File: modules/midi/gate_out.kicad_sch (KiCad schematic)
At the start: 5 parts

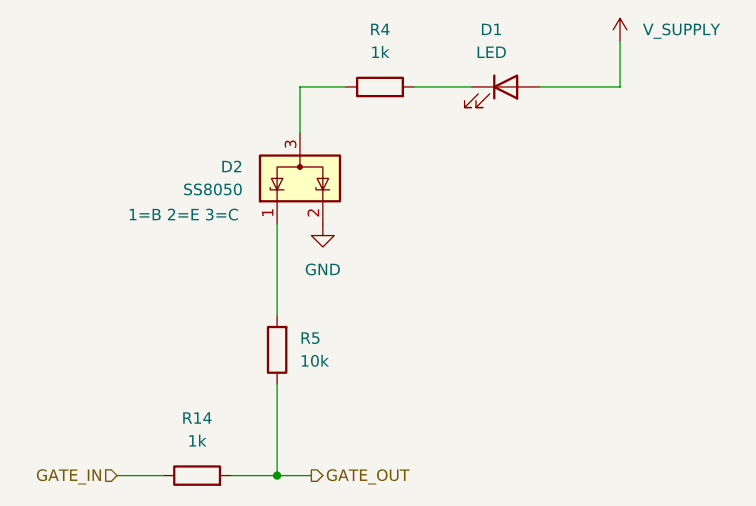
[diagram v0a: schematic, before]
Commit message: midi: Add support to select MIDI A or B
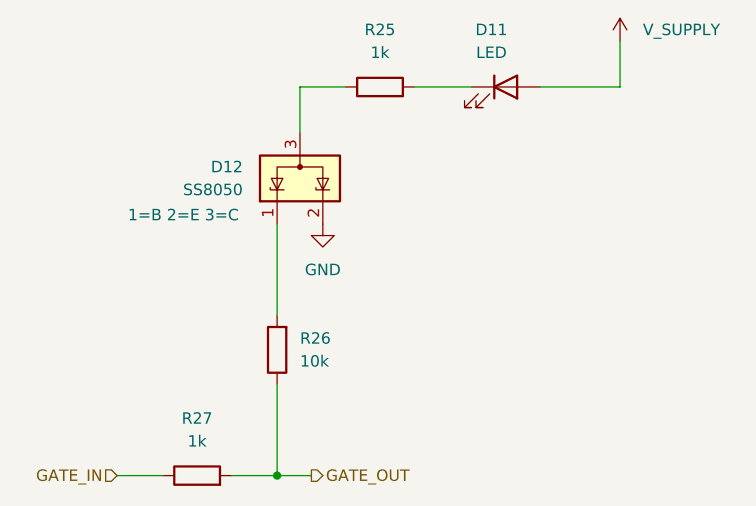
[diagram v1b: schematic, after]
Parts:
- renumbered D1 to D11, D2 to D12, R4 to R25, R5 to R26, R14 to R27
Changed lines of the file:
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@@
 		(dnp no)
 		(fields_autoplaced yes)
-		(property "Reference" "R14"
+		(property "Reference" "R27"
 			(at 66.04 81.28 90)
 			(effects
@@
 		(dnp no)
 		(fields_autoplaced yes)
-		(property "Reference" "R4"
+		(property "Reference" "R25"
 			(at 86.36 38.1 90)
 			(effects
@@
 		(dnp no)
 		(fields_autoplaced yes)
-		(property "Reference" "#PWR011"
+		(property "Reference" "#PWR018"
 			(at 113.03 43.18 0)
 			(effects
@@
 		(dnp no)
 		(fields_autoplaced yes)
-		(property "Reference" "D1"
+		(property "Reference" "D11"
 			(at 98.7425 38.1 0)
 			(effects
@@
 		(on_board yes)
 		(dnp no)
-		(property "Reference" "#PWR012"
+		(property "Reference" "#PWR019"
 			(at 80.01 66.04 0)
 			(effects
@@
 		(on_board yes)
 		(dnp no)
-		(property "Reference" "D2"
+		(property "Reference" "D12"
 			(at 71.12 53.3399 0)
 			(effects
@@
 		(dnp no)
 		(fields_autoplaced yes)
-		(property "Reference" "R5"
+		(property "Reference" "R26"
 			(at 77.47 72.3899 0)
 			(effects
